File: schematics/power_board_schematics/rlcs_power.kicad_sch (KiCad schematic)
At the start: 51 parts, among them J1 Conn_01x05_Male, J2 Conn_01x05_Male, J3 SD_Card, J4 Battery Conn, J5 Battery Conn, J6 CONN_01X02, J7 CONN_01X02, J8 CONN_01X02, Q1 Q_NPN_BEC, Q2 Q_NPN_BEC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

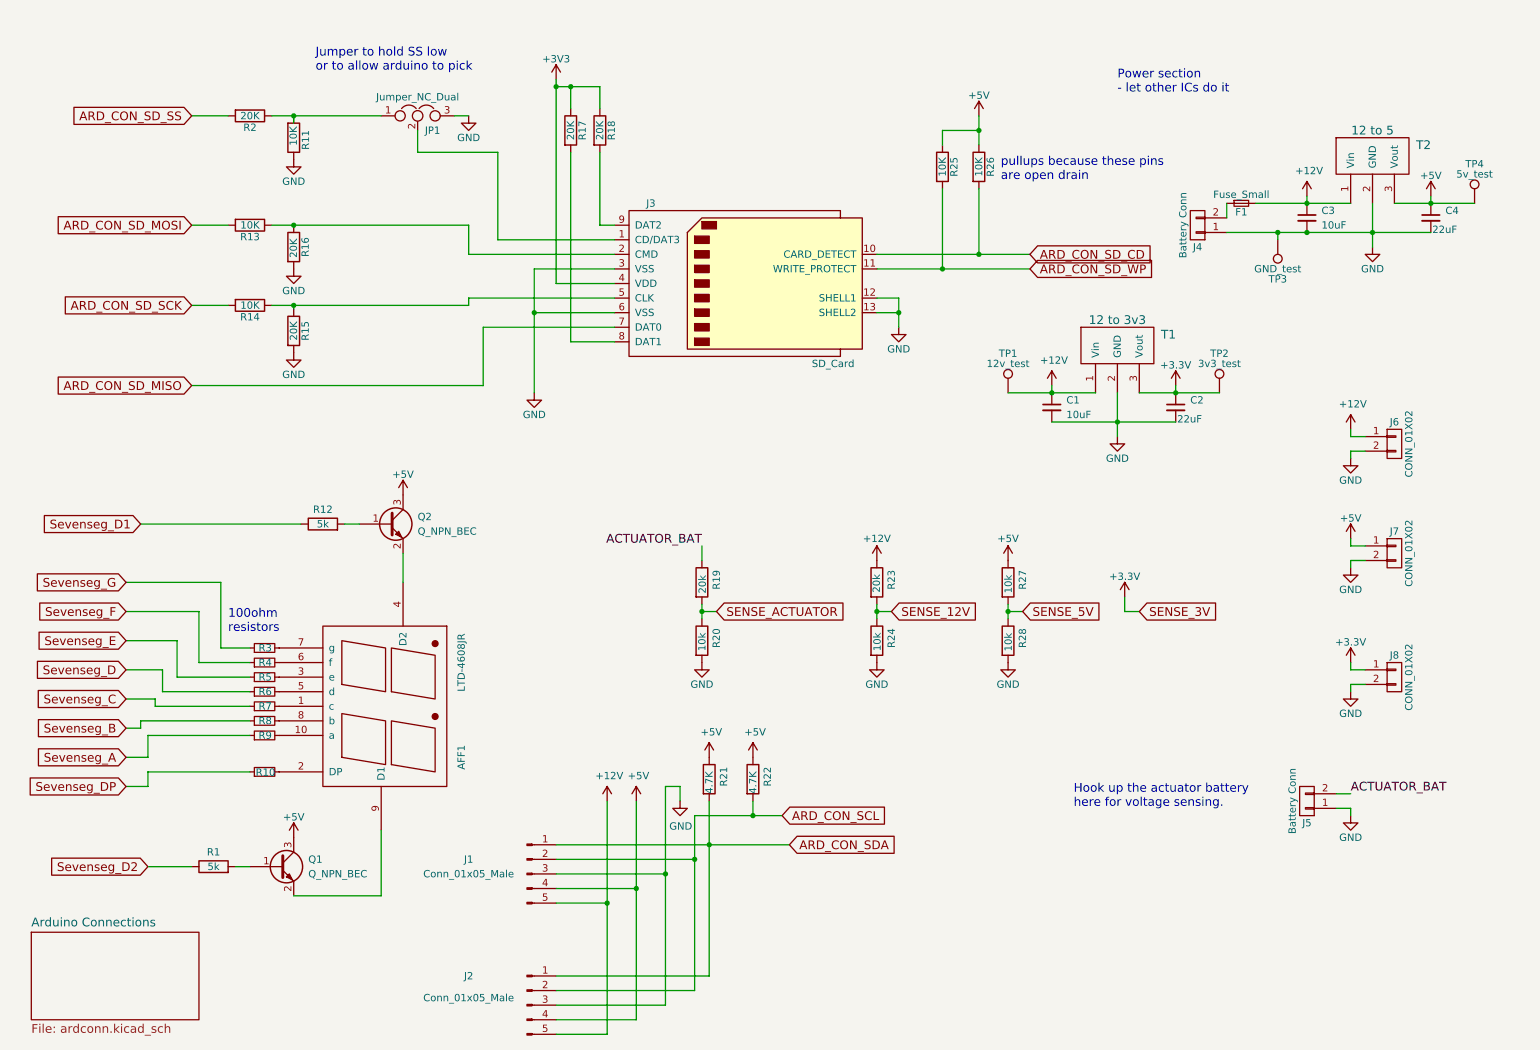
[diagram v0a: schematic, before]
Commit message: Make 12V traces support higher current, review fixes
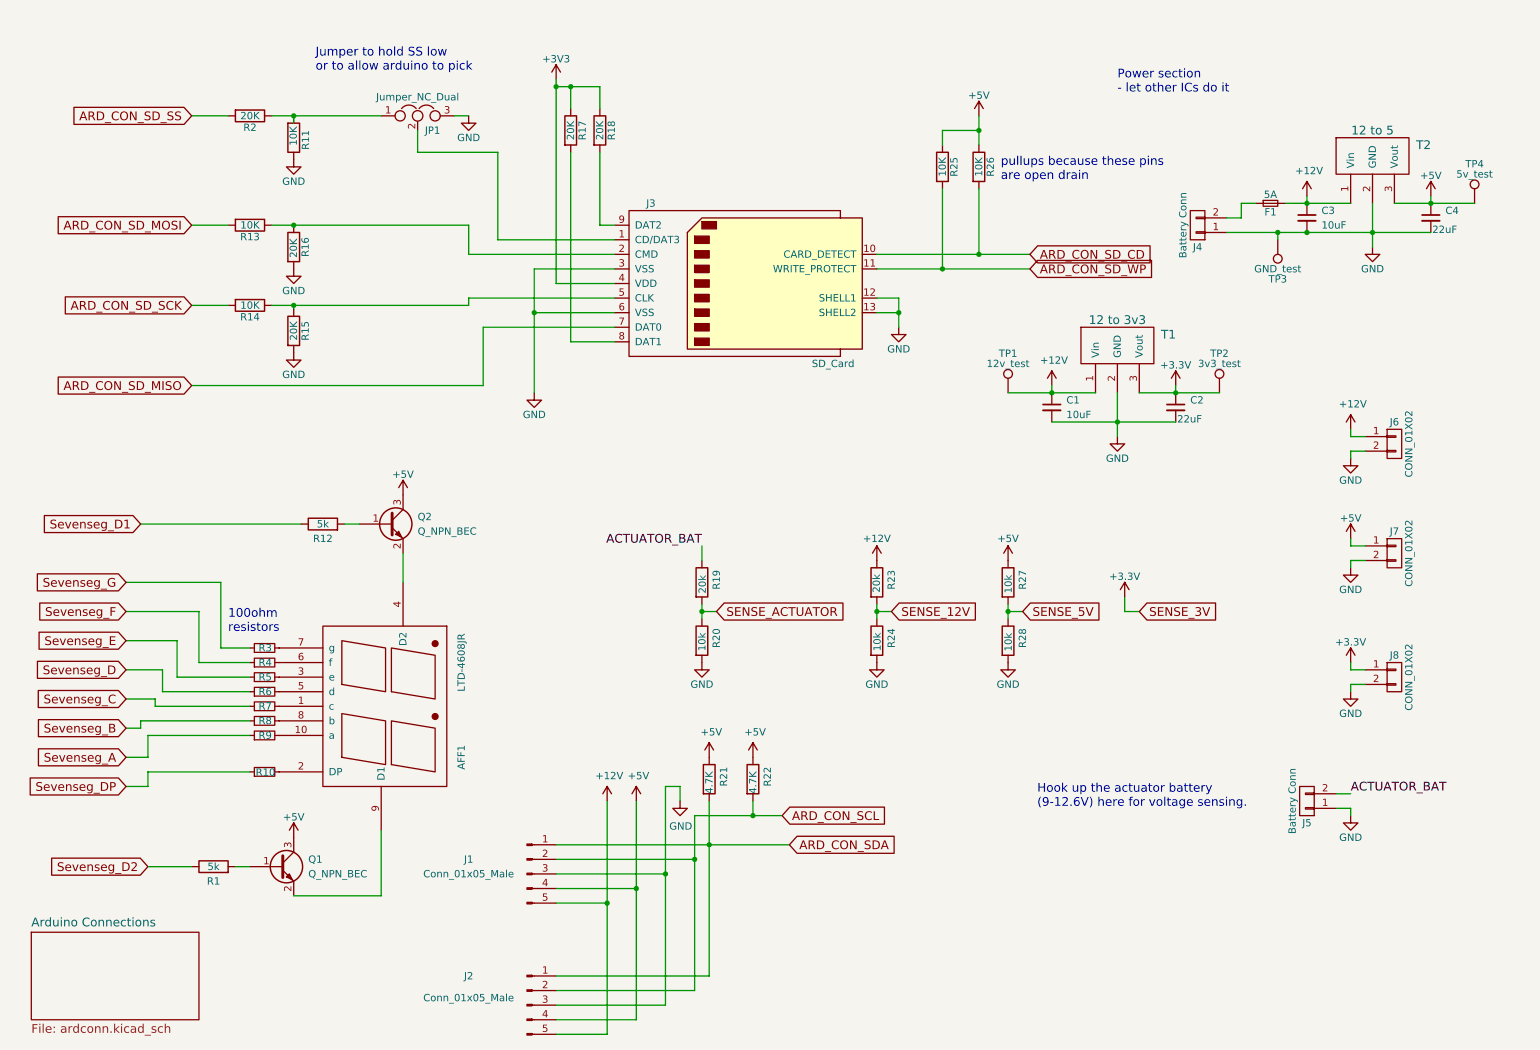
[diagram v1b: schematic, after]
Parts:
- F1: value Fuse_Small -> 5A
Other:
- note added: "Hook up the actuator battery (9-12.6V) here for voltage sensing."
- note removed: "Hook up the actuator battery here for voltage sensing."
- moved on the sheet: F1
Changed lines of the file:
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@@
+    (stroke (width 0) (type default) (color 0 0 0 0))
+  )
+  (wire (pts (xy 232.41 46.99) (xy 234.95 46.99))
     (stroke (width 0) (type default) (color 0 0 0 0))
   )
@@
     (stroke (width 0) (type default) (color 0 0 0 0))
   )
-  (wire (pts (xy 229.87 46.99) (xy 229.87 49.53))
-    (stroke (width 0) (type default) (color 0 0 0 0))
-  )
   (wire (pts (xy 59.69 129.54) (xy 46.99 129.54))
     (stroke (width 0) (type default) (color 0 0 0 0))
@@
     (stroke (width 0) (type default) (color 0 0 0 0))
   )
+  (wire (pts (xy 232.41 49.53) (xy 232.41 46.99))
+    (stroke (width 0) (type default) (color 0 0 0 0))
+  )
   (wire (pts (xy 238.76 52.07) (xy 243.84 52.07))
     (stroke (width 0) (type default) (color 0 0 0 0))
@@
     (stroke (width 0) (type default) (color 0 0 0 0))
   )
-  (wire (pts (xy 234.95 46.99) (xy 243.84 46.99))
+  (wire (pts (xy 240.03 46.99) (xy 243.84 46.99))
     (stroke (width 0) (type default) (color 0 0 0 0))
   )
@@
     (stroke (width 0) (type default) (color 0 0 0 0))
   )
+  (wire (pts (xy 229.87 49.53) (xy 232.41 49.53))
+    (stroke (width 0) (type default) (color 0 0 0 0))
+  )
   (wire (pts (xy 95.25 31.75) (xy 97.79 31.75))
     (stroke (width 0) (type default) (color 0 0 0 0))
@@
     (stroke (width 0) (type default) (color 0 0 0 0))
   )
-  (text "Hook up the actuator battery\nhere for voltage sensing."
-    (at 203.2 152.4 0)
+  (text "Hook up the actuator battery\n(9-12.6V) here for voltage sensing."
+    (at 196.85 152.4 0)
     (effects (font (size 1.524 1.524)) (justify left bottom))
   )
@@
     (pin "2")
   )
-  (symbol (lib_id "Device:Fuse_Small") (at 232.41 46.99 0) (unit 1)
-    (in_bom yes) (on_board yes)
-    (property "Reference" "F1" (id 0) (at 232.41 48.514 0))
-    (property "Value" "Fuse_Small" (id 1) (at 232.41 45.466 0))
-    (property "Footprint" "Fuse_Holders_and_Fuses:Fuseholder5x20_horiz_open_inline_Type-I" (id 2) (at 232.41 46.99 0)
-      (effects (font (size 1.27 1.27)) hide)
-    )
-    (property "Datasheet" "" (id 3) (at 232.41 46.99 0)
+  (symbol (lib_id "Device:Fuse_Small") (at 237.49 46.99 0) (unit 1)
+    (in_bom yes) (on_board yes)
+    (property "Reference" "F1" (id 0) (at 237.49 48.514 0))
+    (property "Value" "5A" (id 1) (at 237.49 45.466 0))
+    (property "Footprint" "Fuse_Holders_and_Fuses:Fuseholder5x20_horiz_open_inline_Type-I" (id 2) (at 237.49 46.99 0)
+      (effects (font (size 1.27 1.27)) hide)
+    )
+    (property "Datasheet" "" (id 3) (at 237.49 46.99 0)
       (effects (font (size 1.27 1.27)) hide)
     )
@@
   (symbol (lib_id "power:GND") (at 67.31 58.42 0) (unit 1)
     (in_bom yes) (on_board yes)
-    (property "Reference" "#PWR?" (id 0) (at 67.31 64.77 0)
+    (property "Reference" "#PWR0101" (id 0) (at 67.31 64.77 0)
       (effects (font (size 1.27 1.27)) hide)
     )
@@
   (symbol (lib_id "Device:R") (at 53.34 162.56 90) (unit 1)
     (in_bom yes) (on_board yes)
-    (property "Reference" "R1" (id 0) (at 53.34 160.02 90))
+    (property "Reference" "R1" (id 0) (at 53.34 165.1 90))
     (property "Value" "5k" (id 1) (at 53.34 162.56 90))
     (property "Footprint" "Resistor_SMD:R_0805_2012Metric_Pad1.20x1.40mm_HandSolder" (id 2) (at 53.34 164.338 90)
@@
   (symbol (lib_id "Device:R") (at 72.39 102.87 90) (unit 1)
     (in_bom yes) (on_board yes)
-    (property "Reference" "R12" (id 0) (at 72.39 100.33 90))
+    (property "Reference" "R12" (id 0) (at 72.39 105.41 90))
     (property "Value" "5k" (id 1) (at 72.39 102.87 90))
     (property "Footprint" "Resistor_SMD:R_0805_2012Metric_Pad1.20x1.40mm_HandSolder" (id 2) (at 72.39 104.648 90)
@@
     )
     (path "/0a27110d-5367-4bc6-bb73-fd6a235d150c"
-      (reference "#PWR?") (unit 1) (value "GND") (footprint "")
+      (reference "#PWR0101") (unit 1) (value "GND") (footprint "")
     )
     (path "/00000000-0000-0000-0000-000059c5bada"
@@
     )
     (path "/00000000-0000-0000-0000-000059b5bfb2"
-      (reference "F1") (unit 1) (value "Fuse_Small") (footprint "Fuse_Holders_and_Fuses:Fuseholder5x20_horiz_open_inline_Type-I")
+      (reference "F1") (unit 1) (value "5A") (footprint "Fuse_Holders_and_Fuses:Fuseholder5x20_horiz_open_inline_Type-I")
     )
     (path "/00000000-0000-0000-0000-00005ee77e1a"

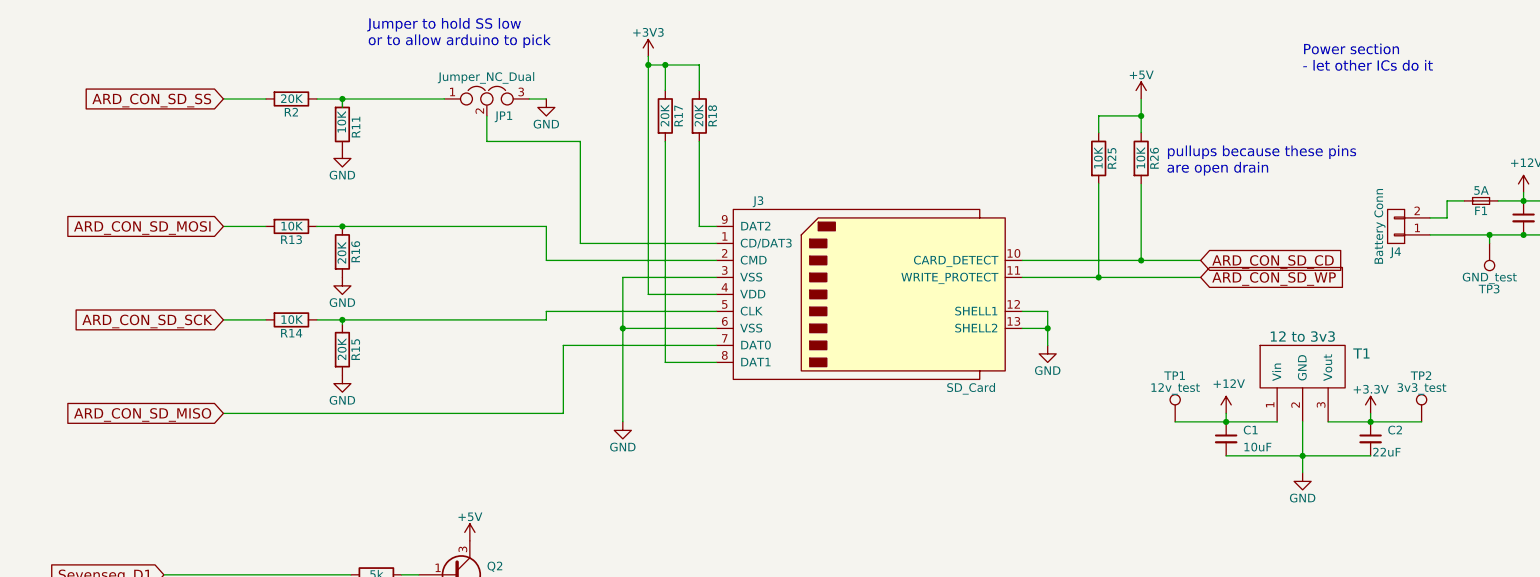
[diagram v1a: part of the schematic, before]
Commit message: Remove SD Card from Towerside Power Board
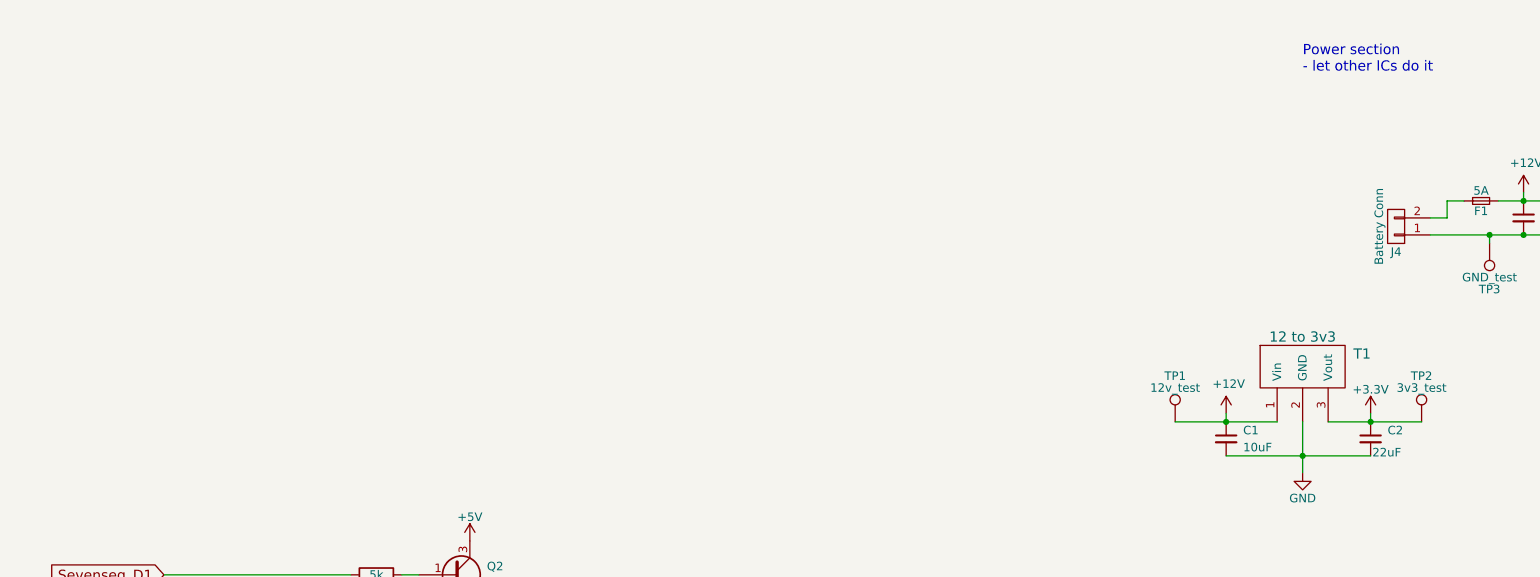
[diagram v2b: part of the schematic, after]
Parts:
- removed J3: SD_Card, rlcs_power_footprints:SDCARD, symbol rlcs_power-rescue:SD_Card
- removed JP1: Jumper_NC_Dual, Connector_PinHeader_2.54mm:PinHeader_1x03_P2.54mm_Vertical, symbol Device:Jumper_NC_Dual
- removed R11, R13, R14, R25, R26: 10K, Resistor_SMD:R_0805_2012Metric_Pad1.20x1.40mm_HandSolder, symbol Device:R
- removed R15, R16, R17, R18, R2: 20K, Resistor_SMD:R_0805_2012Metric_Pad1.20x1.40mm_HandSolder, symbol Device:R
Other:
- note removed: "Jumper to hold SS low or to allow arduino to pick"
- note removed: "pullups because these pins are open drain"
